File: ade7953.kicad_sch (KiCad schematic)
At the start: 57 parts, among them U2 ADE7953xCP, Y1 3.58MHz

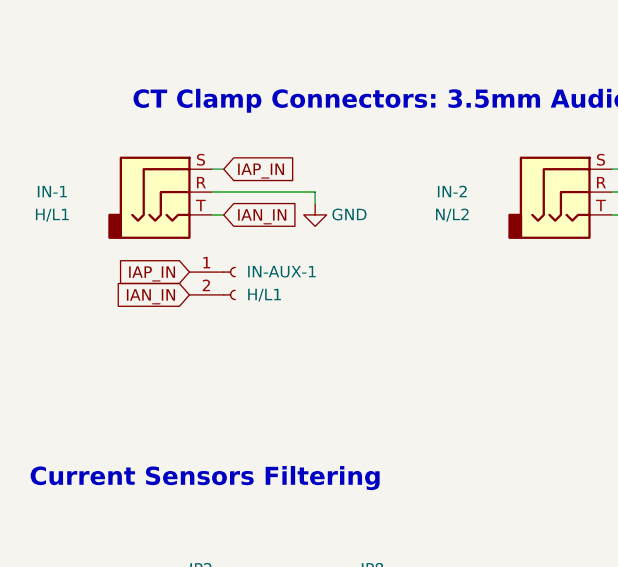
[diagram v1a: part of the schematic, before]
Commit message: unpopulate headers that are not needed
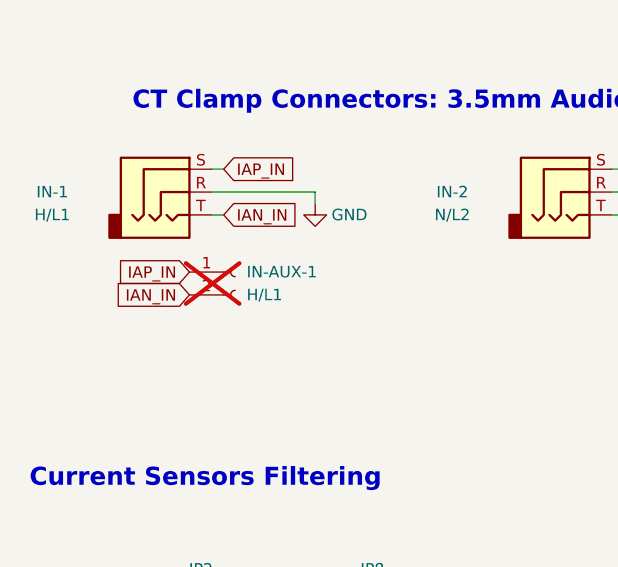
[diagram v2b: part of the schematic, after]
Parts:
- IN-AUX-1: now not fitted; now left out of the parts list
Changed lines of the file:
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@@
 		(unit 1)
 		(exclude_from_sim no)
-		(in_bom yes)
+		(in_bom no)
 		(on_board yes)
-		(dnp no)
+		(dnp yes)
 		(fields_autoplaced yes)
 		(property "Reference" "IN-AUX-1"

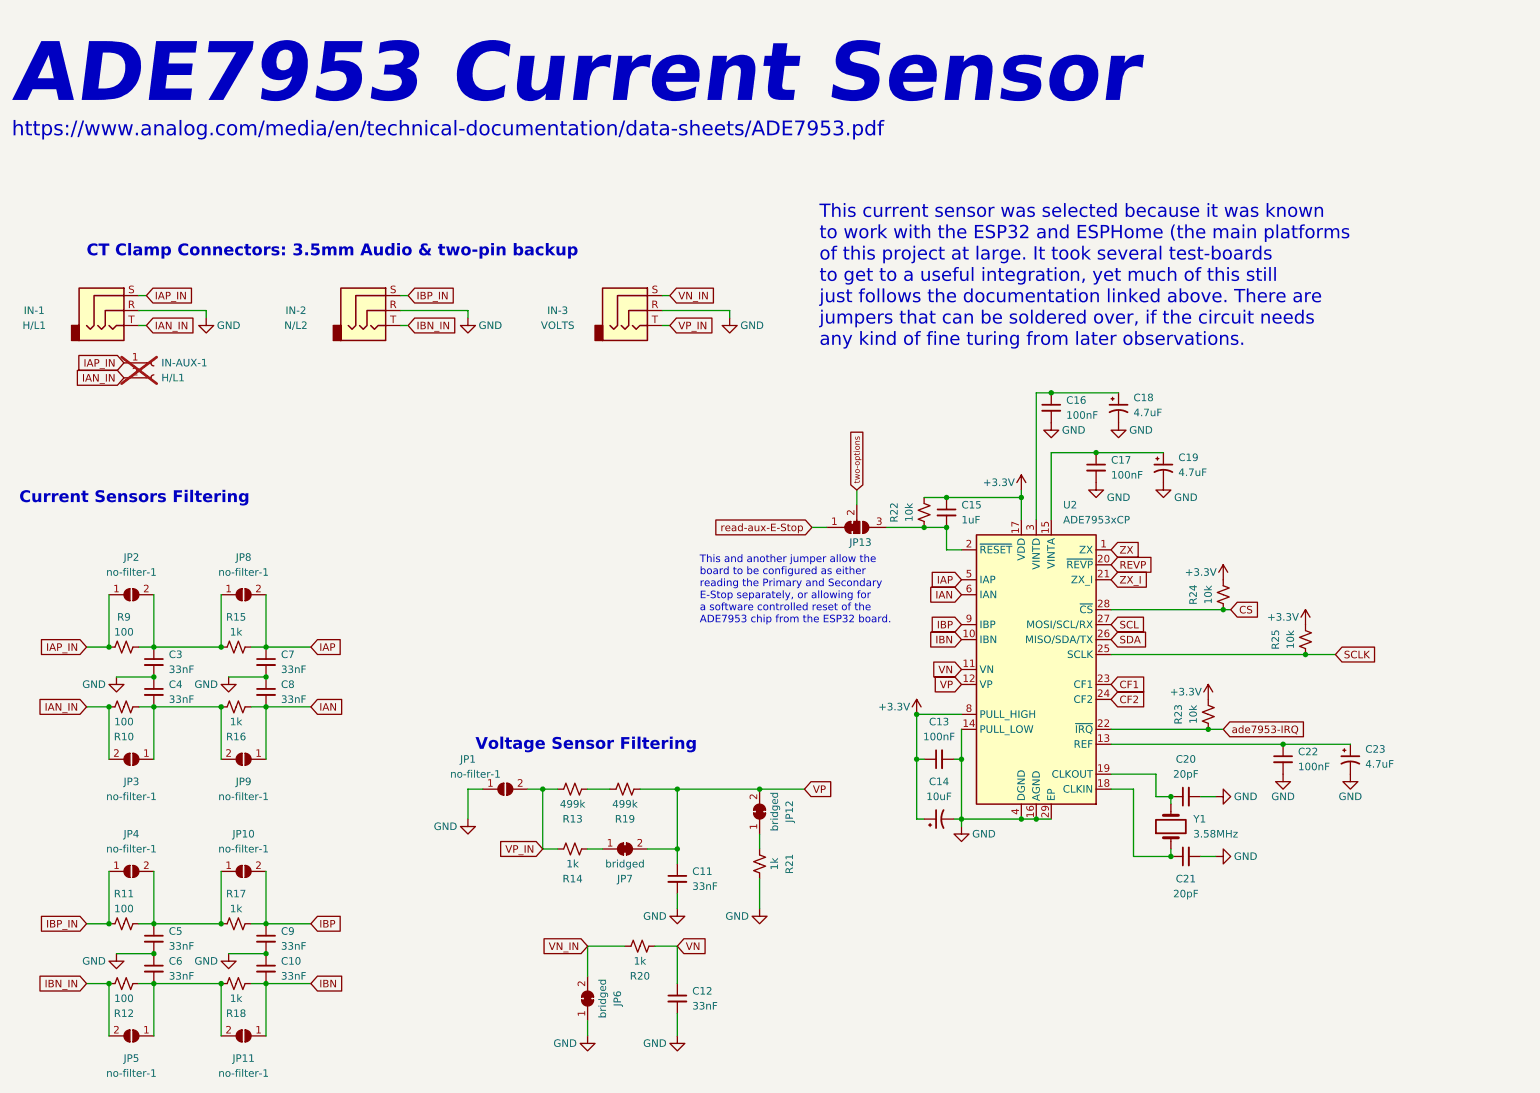
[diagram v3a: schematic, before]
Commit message: moved LED GPIO to fit free pins for ethernet wing
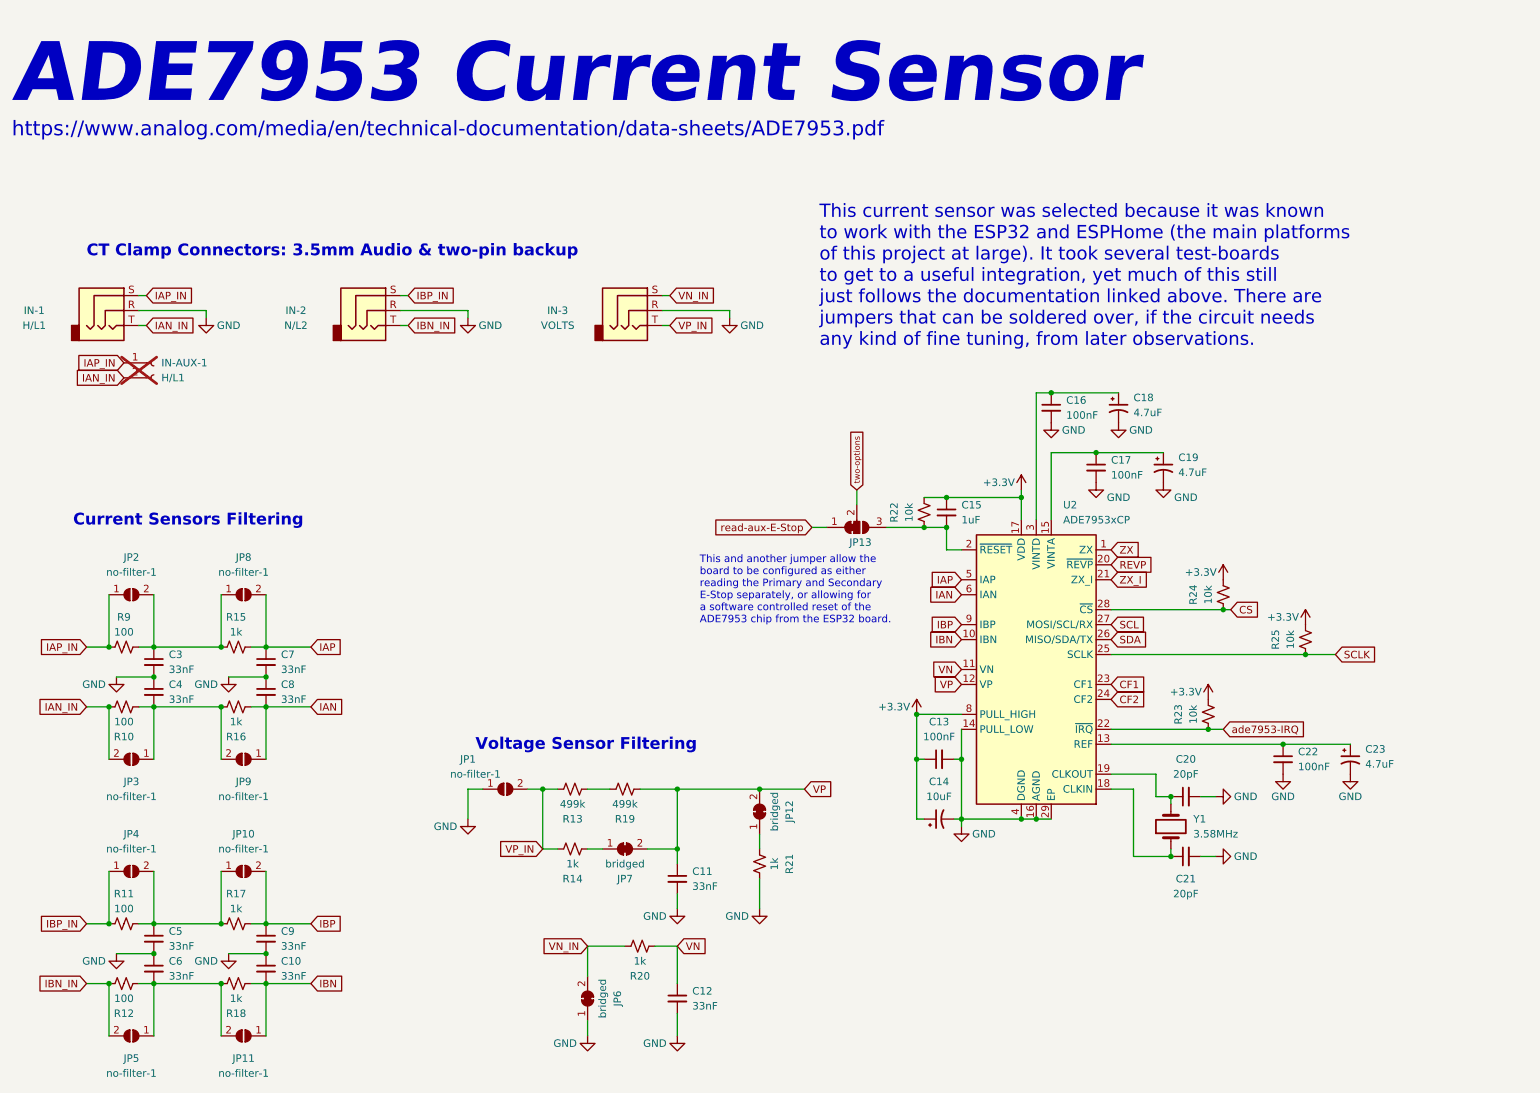
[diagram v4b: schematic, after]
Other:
- note added: "This current sensor was selected because it was known to work with the ESP32 and ESPHome (the main platforms of this project at large). It took several test-boards to get to a useful integration, yet much of this still just follows the documentation linked above. There are jumpers that can be soldered over, if the circuit needs any kind of fine tuning, from later observations."
- note removed: "This current sensor was selected because it was known to work with the ESP32 and ESPHome (the main platforms of this project at large. It took several test-boards to get to a useful integration, yet much of this still just follows the documentation linked above. There are jumpers that can be soldered over, if the circuit needs any kind of fine turing from later observations."
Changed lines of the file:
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@@
 	(title_block
 		(title "ADE7953 Current Sensor")
-		(date "2022-10-09")
+		(date "2024-12-13")
 		(rev "3")
 		(company "Corey Rice & MakeHaven")
@@
 			)
 			(justify left bottom)
+			(href "https://www.analog.com/media/en/technical-documentation/data-sheets/ADE7953.pdf")
 		)
 	)
@@
 		)
 	)
-	(text "This current sensor was selected because it was known \nto work with the ESP32 and ESPHome (the main platforms \nof this project at large. It took several test-boards \nto get to a useful integration, yet much of this still\njust follows the documentation linked above. There are \njumpers that can be soldered over, if the circuit needs\nany kind of fine turing from later observations."
+	(text "This current sensor was selected because it was known \nto work with the ESP32 and ESPHome (the main platforms \nof this project at large). It took several test-boards \nto get to a useful integration, yet much of this still\njust follows the documentation linked above. There are \njumpers that can be soldered over, if the circuit needs\nany kind of fine tuning, from later observations."
 		(exclude_from_sim no)
 		(at 157.48 71.12 0)
@@
 	(text "Current Sensors Filtering"
 		(exclude_from_sim no)
-		(at 21.59 97.79 0)
+		(at 30.734 101.6 0)
 		(effects
 			(font

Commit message: ordered B1P3 test run from JLCPCB
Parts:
- renumbered IN-1 to J6, IN-2 to J7, IN-3 to J8
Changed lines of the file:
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@@
 		(on_board yes)
 		(dnp no)
-		(property "Reference" "IN-2"
+		(property "Reference" "J7"
 			(at 68.58 64.77 0)
 			(effects
@@
 			(project "wing-combo"
 				(path "/586efc0f-7de2-49a7-ac21-ecfef2f716d6/3f0e9b91-fe15-47d5-84d6-aa71b368b91e/03adfa84-7245-4a0a-b28d-db7d09a8f743"
-					(reference "IN-2")
+					(reference "J7")
 					(unit 1)
 				)
@@
 		(on_board yes)
 		(dnp no)
-		(property "Reference" "IN-3"
+		(property "Reference" "J8"
 			(at 113.03 64.77 0)
 			(effects
@@
 			(project "wing-combo"
 				(path "/586efc0f-7de2-49a7-ac21-ecfef2f716d6/3f0e9b91-fe15-47d5-84d6-aa71b368b91e/03adfa84-7245-4a0a-b28d-db7d09a8f743"
-					(reference "IN-3")
+					(reference "J8")
 					(unit 1)
 				)
@@
 		(on_board yes)
 		(dnp no)
-		(property "Reference" "IN-1"
+		(property "Reference" "J6"
 			(at 24.13 64.77 0)
 			(effects
@@
 			(project "wing-combo"
 				(path "/586efc0f-7de2-49a7-ac21-ecfef2f716d6/3f0e9b91-fe15-47d5-84d6-aa71b368b91e/03adfa84-7245-4a0a-b28d-db7d09a8f743"
-					(reference "IN-1")
+					(reference "J6")
 					(unit 1)
 				)

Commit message: cleanup
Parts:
- added binary-current: Conn_01x03_Female, Connector_JST:JST_PH_B3B-PH-K_1x03_P2.00mm_Vertical, symbol Connector:Conn_01x03_Female
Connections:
- net GND: now also binary-current.3 (Pin_3)
- new net +3.3VA: binary-current.1 (Pin_1)
- new net binary-current: binary-current.2 (Pin_2)
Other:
- note added: "Backup Plan"
- note added: "connect a breakout board with simple i/o"

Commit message: [auto] annotate schematic
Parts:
- renumbered binary-current to binary-current1
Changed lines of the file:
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@@
 		(on_board yes)
 		(dnp no)
-		(property "Reference" "binary-current"
+		(property "Reference" "binary-current1"
 			(at 102.616 100.33 0)
 			(effects
@@
 			(project "wing-combo"
 				(path "/586efc0f-7de2-49a7-ac21-ecfef2f716d6/3f0e9b91-fe15-47d5-84d6-aa71b368b91e/03adfa84-7245-4a0a-b28d-db7d09a8f743"
-					(reference "binary-current")
+					(reference "binary-current1")
 					(unit 1)
 				)

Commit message: 1.4.1 schematic update
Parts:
- IN-AUX-1: symbol Connector:Conn_01x02_Female -> Connector:Conn_01x02_Socket; now in the parts list
- J6, J7, J8: symbol Connector:AudioJack3 -> Connector_Audio:AudioJack3
- binary-current1: symbol Connector:Conn_01x03_Female -> Connector:Conn_01x03_Socket
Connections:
- net +3.3VA is gone; now on net +3.3V: binary-current1.1 (Pin_1)
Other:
- note added: "The ADE7953 can be tricky to fully implement, and we know that an old CT Clamp breakout board has worked for years. For that reason, we added this 'backup plan' header to easily attach a binary current sensor in the event that you need a fallback."
